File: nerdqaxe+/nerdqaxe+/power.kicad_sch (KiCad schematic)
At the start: 94 parts, among them J3 Conn_01x01, J4 Conn_01x01, U3 TPS53647, U36 MCP1824T-1802E, U4 CSD95472Q5MC, U5 CSD95472Q5MC, U6 AP3211, U7 MCP1824T-0802E

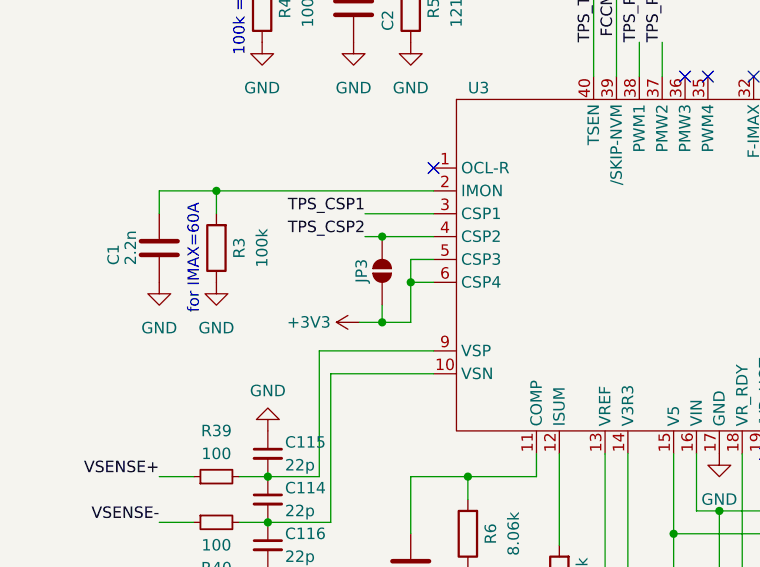
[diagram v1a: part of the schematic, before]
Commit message: removed ph2-dis solderjumper because it's not needed
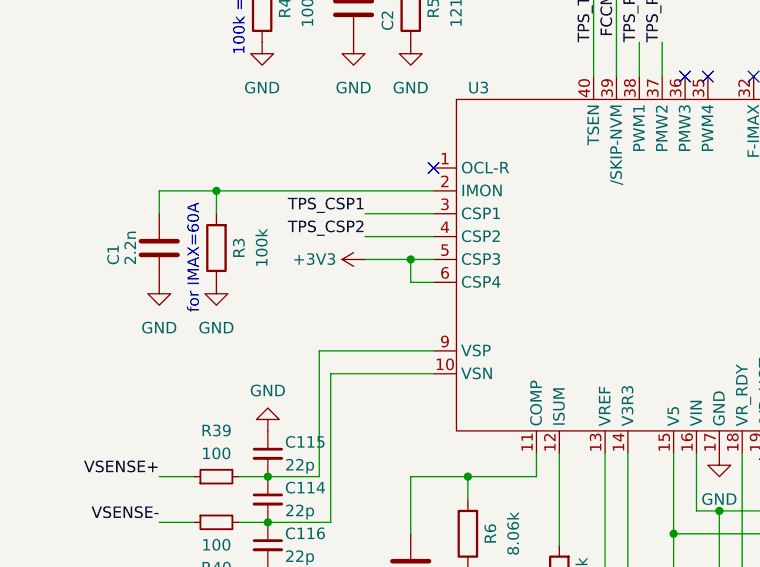
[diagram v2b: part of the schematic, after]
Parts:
- removed JP3: SolderJumper_2_Open, Jumper:SolderJumper-2_P1.3mm_Open_RoundedPad1.0x1.5mm, symbol Jumper:SolderJumper_2_Open
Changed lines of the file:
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@@
 	)
 	(junction
+		(at 62.23 120.65)
+		(diameter 0)
+		(color 0 0 0 0)
+	)
+	(junction
 		(at 233.045 257.175)
 		(diameter 0)
@@
 	)
 	(junction
-		(at 59.055 118.11)
-		(diameter 0)
-		(color 0 0 0 0)
-	)
-	(junction
 		(at 294.64 105.41)
 		(diameter 0)
@@
 	)
 	(junction
-		(at 62.23 123.19)
-		(diameter 0)
-		(color 0 0 0 0)
-	)
-	(junction
 		(at 381 120.65)
 		(diameter 0)
@@
 	)
 	(junction
-		(at 59.055 127.635)
-		(diameter 0)
-		(color 0 0 0 0)
-	)
-	(junction
 		(at 364.49 120.65)
 		(diameter 0)
@@
 	(wire
 		(pts
-			(xy 59.055 125.73) (xy 59.055 127.635)
-		)
-		(stroke
-			(width 0)
-			(type default)
-		)
-	)
-	(wire
-		(pts
 			(xy 294.64 109.22) (xy 294.64 105.41)
 		)
@@
 	(wire
 		(pts
-			(xy 62.23 127.635) (xy 59.055 127.635)
+			(xy 57.15 120.65) (xy 62.23 120.65)
 		)
 		(stroke
@@
 	(wire
 		(pts
-			(xy 62.23 120.65) (xy 62.23 123.19)
-		)
-		(stroke
-			(width 0)
-			(type default)
-		)
-	)
-	(wire
-		(pts
 			(xy 85.09 85.09) (xy 85.09 100.33)
 		)
@@
 	(wire
 		(pts
-			(xy 59.055 127.635) (xy 56.515 127.635)
-		)
-		(stroke
-			(width 0)
-			(type default)
-		)
-	)
-	(wire
-		(pts
 			(xy 64.77 113.03) (xy 40.64 113.03)
 		)
@@
 	(wire
 		(pts
-			(xy 57.15 118.11) (xy 59.055 118.11)
+			(xy 57.15 118.11) (xy 64.77 118.11)
 		)
 		(stroke
@@
 	(wire
 		(pts
-			(xy 59.055 118.11) (xy 64.77 118.11)
-		)
-		(stroke
-			(width 0)
-			(type default)
-		)
-	)
-	(wire
-		(pts
 			(xy 145.415 243.205) (xy 145.415 259.715)
 		)
@@
 	(wire
 		(pts
-			(xy 62.23 123.19) (xy 62.23 127.635)
+			(xy 62.23 120.65) (xy 62.23 123.19)
 		)
 		(stroke
@@
 		(lib_name "+3V3_2")
 		(lib_id "power:+3V3")
-		(at 56.515 127.635 90)
+		(at 57.15 120.65 90)
 		(unit 1)
 		(exclude_from_sim no)
@@
 		(fields_autoplaced yes)
 		(property "Reference" "#PWR05"
-			(at 60.325 127.635 0)
+			(at 60.96 120.65 0)
 			(effects
 				(font
@@
 		)
 		(property "Value" "+3V3"
-			(at 53.34 127.6349 90)
+			(at 53.975 120.6499 90)
 			(effects
 				(font
@@
 		)
 		(property "Footprint" ""
-			(at 56.515 127.635 0)
+			(at 57.15 120.65 0)
 			(effects
 				(font
@@
 		)
 		(property "Datasheet" ""
-			(at 56.515 127.635 0)
+			(at 57.15 120.65 0)
 			(effects
 				(font
@@
 		)
 		(property "Description" "Power symbol creates a global label with name \"+3V3\""
-			(at 56.515 127.635 0)
+			(at 57.15 120.65 0)
 			(effects
 				(font
@@
 					(unit 1)
 				)
-			)
-		)
-	)
-	(symbol
-		(lib_id "Jumper:SolderJumper_2_Open")
-		(at 59.055 121.92 90)
-		(unit 1)
-		(exclude_from_sim yes)
-		(in_bom no)
-		(on_board yes)
-		(dnp no)
-		(property "Reference" "JP3"
-			(at 56.769 121.92 0)
-			(effects
-				(font
-					(size 1.27 1.27)
-				)
-			)
-		)
-		(property "Value" "SolderJumper_2_Open"
-			(at 55.245 121.92 0)
-			(effects
-				(font
-					(size 1.27 1.27)
-				)
-				(hide yes)
-			)
-		)
-		(property "Footprint" "Jumper:SolderJumper-2_P1.3mm_Open_RoundedPad1.0x1.5mm"
-			(at 59.055 121.92 0)
-			(effects
-				(font
-					(size 1.27 1.27)
-				)
-				(hide yes)
-			)
-		)
-		(property "Datasheet" "~"
-			(at 59.055 121.92 0)
-			(effects
-				(font
-					(size 1.27 1.27)
-				)
-				(hide yes)
-			)
-		)
-		(property "Description" "Solder Jumper, 2-pole, open"
-			(at 59.055 121.92 0)
-			(effects
-				(font
-					(size 1.27 1.27)
-				)
-				(hide yes)
-			)
-		)
-		(property "Distributor" "-"
-			(at 59.055 121.92 0)
-			(effects
-				(font
-					(size 1.27 1.27)
-				)
-				(hide yes)
-			)
-		)
-		(pin "2"
-		)
-		(pin "1"
-		)
-		(instances
-			(project "nerdqaxe+"
-				(path "/e63e39d7-6ac0-4ffd-8aa3-1841a4541b55/8ec0a9c6-2b78-44ef-a83d-9047d2828409"
-					(reference "JP3")
-					(unit 1)
-				)

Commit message: updated bom of + for 24V cap
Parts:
- C92: Manufacturer 875075355002 -> HHXE250ARA221MHA0G; OrderNr 732-6489-1-ND -> 565-HHXE250ARA221MHA0GCT-ND
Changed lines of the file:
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@@
 (kicad_sch
-	(version 20231120)
+	(version 20250114)
 	(generator "eeschema")
-	(generator_version "8.0")
+	(generator_version "9.0")
 	(paper "A3")
 	(title_block
@@
 		(rev "202")
 	)
+	(text "default\nOff"
+		(exclude_from_sim no)
+		(at 125.73 262.89 0)
+		(effects
+			(font
+				(size 1.27 1.27)
+			)
+		)
+	)
+	(text "for IMAX=60A"
+		(exclude_from_sim no)
+		(at 38.1 120.65 90)
+		(effects
+			(font
+				(size 1.27 1.27)
+			)
+		)
+	)
+	(text "100k = NVM"
+		(exclude_from_sim no)
+		(at 43.18 92.71 90)
+		(effects
+			(font
+				(size 1.27 1.27)
+			)
+		)
+	)
 	(junction
 		(at 302.26 105.41)
@@
 		)
 	)
-	(text "default\nOff"
-		(exclude_from_sim no)
-		(at 125.73 262.89 0)
-		(effects
-			(font
-				(size 1.27 1.27)
-			)
-		)
-	)
-	(text "for IMAX=60A"
-		(exclude_from_sim no)
-		(at 38.1 120.65 90)
-		(effects
-			(font
-				(size 1.27 1.27)
-			)
-		)
-	)
-	(text "100k = NVM"
-		(exclude_from_sim no)
-		(at 43.18 92.71 90)
-		(effects
-			(font
-				(size 1.27 1.27)
-			)
-		)
-	)
 	(label "TPS_PWM1"
 		(at 87.63 96.52 90)
-		(fields_autoplaced yes)
 		(effects
 			(font
@@
 	(label "TPS_CSP1"
 		(at 57.15 115.57 180)
-		(fields_autoplaced yes)
 		(effects
 			(font
@@
 	(label "FCCM"
 		(at 203.2 142.24 180)
-		(fields_autoplaced yes)
 		(effects
 			(font
@@
 	(label "{slash}RESET"
 		(at 125.73 133.35 0)
-		(fields_autoplaced yes)
 		(effects
 			(font
@@
 	(label "TPS_TSEN"
 		(at 82.55 96.52 90)
-		(fields_autoplaced yes)
 		(effects
 			(font
@@
 	(label "TPS_TSEN"
 		(at 252.73 102.87 0)
-		(fields_autoplaced yes)
 		(effects
 			(font
@@
 	(label "TPS_PWM1"
 		(at 214.63 96.52 180)
-		(fields_autoplaced yes)
 		(effects
 			(font
@@
 	(label "FCCM"
 		(at 203.2 99.06 180)
-		(fields_autoplaced yes)
 		(effects
 			(font
@@
 	(label "TPS_PWM2"
 		(at 214.63 139.7 180)
-		(fields_autoplaced yes)
 		(effects
 			(font
@@
 	(label "TPS_CSP2"
 		(at 57.15 118.11 180)
-		(fields_autoplaced yes)
 		(effects
 			(font
@@
 	(label "TPS_PWM2"
 		(at 90.17 96.52 90)
-		(fields_autoplaced yes)
 		(effects
 			(font
@@
 	(label "VSENSE+"
 		(at 34.29 144.78 180)
-		(fields_autoplaced yes)
 		(effects
 			(font
@@
 	(label "VSENSE-"
 		(at 392.43 143.51 0)
-		(fields_autoplaced yes)
 		(effects
 			(font
@@
 	(label "VSENSE-"
 		(at 34.29 149.86 180)
-		(fields_autoplaced yes)
 		(effects
 			(font
@@
 	(label "TPS_CSP2"
 		(at 204.47 154.94 180)
-		(fields_autoplaced yes)
 		(effects
 			(font
@@
 	(label "TPS_CSP1"
 		(at 204.47 111.76 180)
-		(fields_autoplaced yes)
 		(effects
 			(font
@@
 	(label "VSENSE+"
 		(at 392.43 139.7 0)
-		(fields_autoplaced yes)
 		(effects
 			(font
@@
 	(label "TPS_TSEN"
 		(at 252.73 146.05 0)
-		(fields_autoplaced yes)
 		(effects
 			(font
@@
 	(label "FCCM"
 		(at 85.09 95.885 90)
-		(fields_autoplaced yes)
 		(effects
 			(font
@@
 		(shape output)
 		(at 120.65 158.75 0)
-		(fields_autoplaced yes)
 		(effects
 			(font
@@
 		(shape output)
 		(at 31.75 26.67 180)
-		(fields_autoplaced yes)
 		(effects
 			(font
@@
 		(shape input)
 		(at 31.75 29.21 180)
-		(fields_autoplaced yes)
 		(effects
 			(font
@@
 		(shape input)
 		(at 121.92 125.73 0)
-		(fields_autoplaced yes)
 		(effects
 			(font
@@
 		(shape bidirectional)
 		(at 121.92 120.65 0)
-		(fields_autoplaced yes)
 		(effects
 			(font
@@
 		(shape output)
 		(at 31.75 34.29 180)
-		(fields_autoplaced yes)
 		(effects
 			(font
@@
 		(shape output)
 		(at 31.75 31.75 180)
-		(fields_autoplaced yes)
 		(effects
 			(font
@@
 		(shape output)
 		(at 31.75 39.37 180)
-		(fields_autoplaced yes)
 		(effects
 			(font
@@
 		(shape output)
 		(at 31.75 36.83 180)
-		(fields_autoplaced yes)
 		(effects
 			(font
@@
 		(shape input)
 		(at 153.67 128.27 0)
-		(fields_autoplaced yes)
 		(effects
 			(font
@@
 		(shape input)
 		(at 128.905 243.205 180)
-		(fields_autoplaced yes)
 		(effects
 			(font
@@
 			)
 		)
-		(property "Manufacturer" "875075355002"
+		(property "Manufacturer" "HHXE250ARA221MHA0G"
 			(at 360.68 80.01 0)
 			(effects
@@
 			)
 		)
-		(property "OrderNr" "732-6489-1-ND"
+		(property "OrderNr" "565-HHXE250ARA221MHA0GCT-ND"
 			(at 360.68 80.01 0)
 			(effects
@@
 		)
 	)
+	(embedded_fonts no)
 )
